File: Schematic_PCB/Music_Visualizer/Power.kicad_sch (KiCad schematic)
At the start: 38 parts, among them J2 Barrel_Jack_PTH, J6 3.5mm, Q1 DMP2123LQ-7, SW2 SW_SPST, U1 LM324, U2 LM324, U3 LM324, U4 LM324, U5 LM324, U6 LM324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

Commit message: Replace elec. cap.
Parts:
- C54: footprint Capacitor_THT:CP_Radial_D5.0mm_P2.00mm -> Capacitor_SMD:CP_Elec_6.3x5.3
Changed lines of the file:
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@@
 			)
 		)
-		(property "Footprint" "Capacitor_THT:CP_Radial_D5.0mm_P2.00mm"
+		(property "Footprint" "Capacitor_SMD:CP_Elec_6.3x5.3"
 			(at 50.4952 54.61 0)
 			(effects

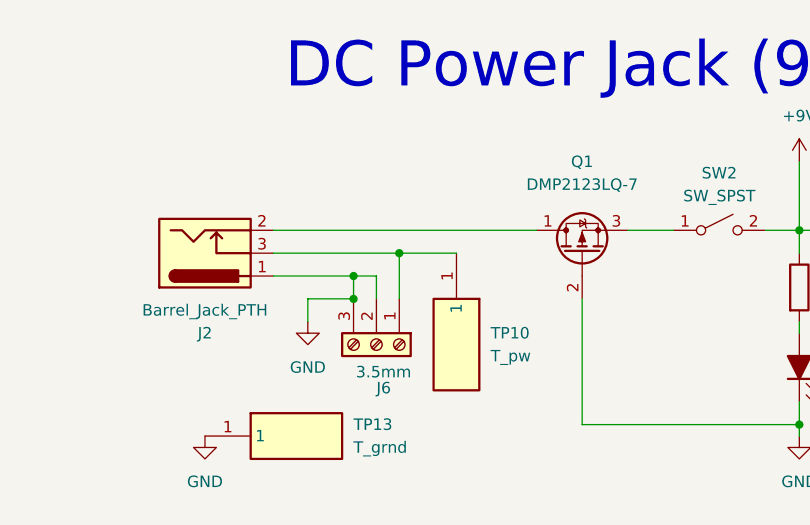
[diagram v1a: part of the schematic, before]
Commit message: Change Barrel jack footprint
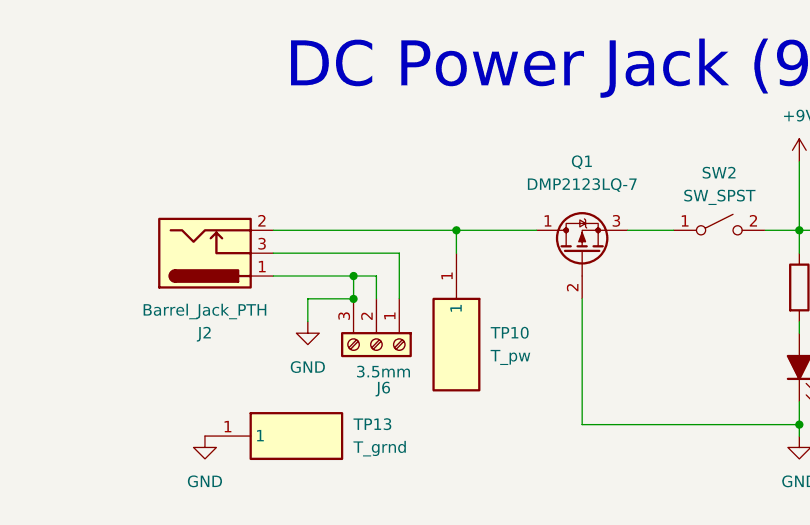
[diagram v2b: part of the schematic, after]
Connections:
- net at J2.2 (GND), Q1.1 (D): now also TP10.1
- net at J2.3 (GNDBREAK), J6.1 (Pin_1): no longer TP10.1
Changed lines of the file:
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@@
+	)
+	(junction
+		(at 172.72 52.07)
+		(diameter 0)
+		(color 0 0 0 0)
 	)
 	(junction
@@
 	)
 	(junction
-		(at 166.37 54.61)
-		(diameter 0)
-		(color 0 0 0 0)
-	)
-	(junction
 		(at 210.82 52.07)
 		(diameter 0)
@@
 	(wire
 		(pts
+			(xy 172.72 52.07) (xy 181.61 52.07)
+		)
+		(stroke
+			(width 0)
+			(type default)
+		)
+	)
+	(wire
+		(pts
 			(xy 191.77 52.07) (xy 196.85 52.07)
 		)
@@
 	(wire
 		(pts
+			(xy 172.72 52.07) (xy 172.72 54.61)
+		)
+		(stroke
+			(width 0)
+			(type default)
+		)
+	)
+	(wire
+		(pts
 			(xy 58.42 99.06) (xy 69.85 99.06)
 		)
@@
 	(wire
 		(pts
-			(xy 152.4 52.07) (xy 181.61 52.07)
+			(xy 152.4 52.07) (xy 172.72 52.07)
 		)
 		(stroke
@@
 		)
 		(stroke
-			(width 0)
-			(type default)
-		)
-	)
-	(wire
-		(pts
-			(xy 166.37 54.61) (xy 172.72 54.61)
-		)
-		(stroke

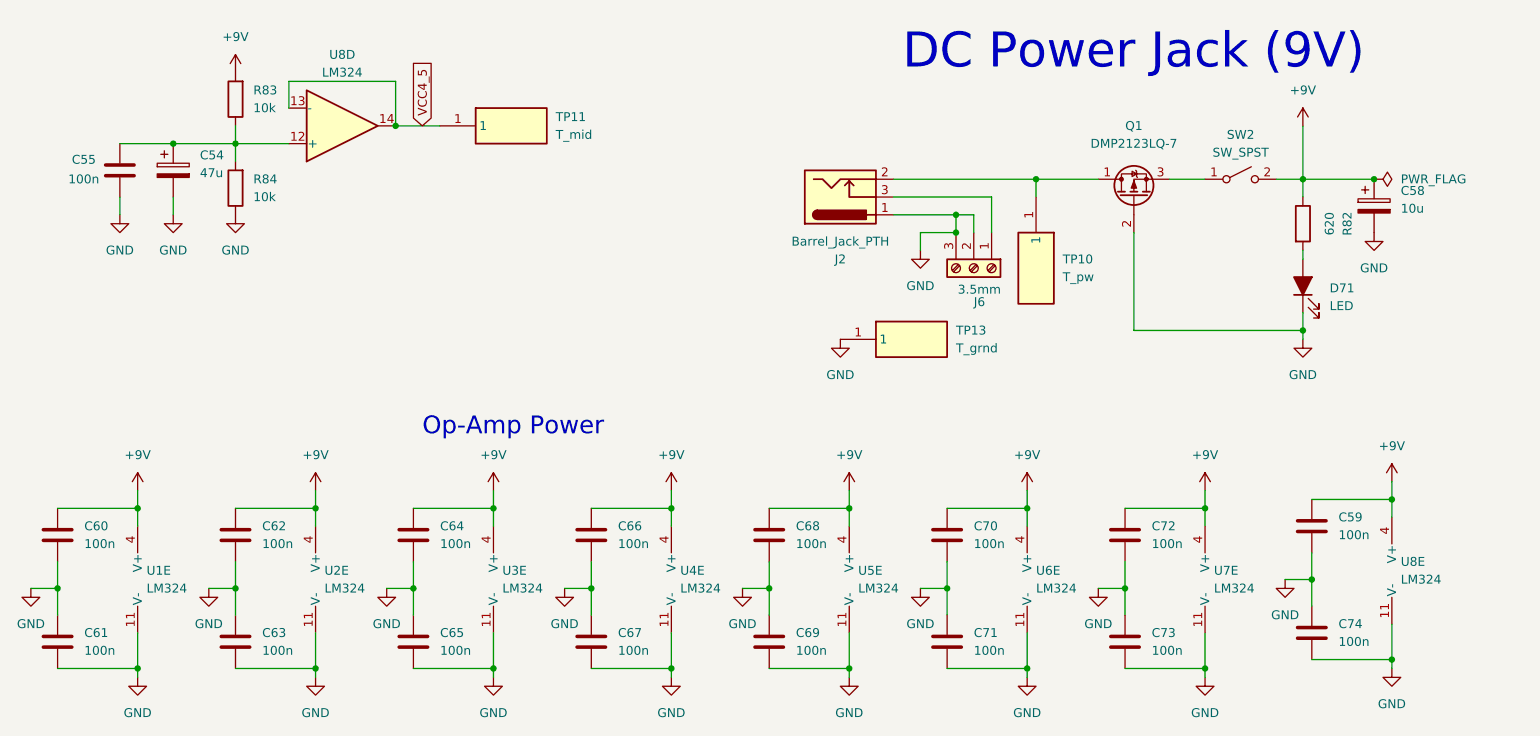
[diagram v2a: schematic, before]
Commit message: Update op amp decoupling
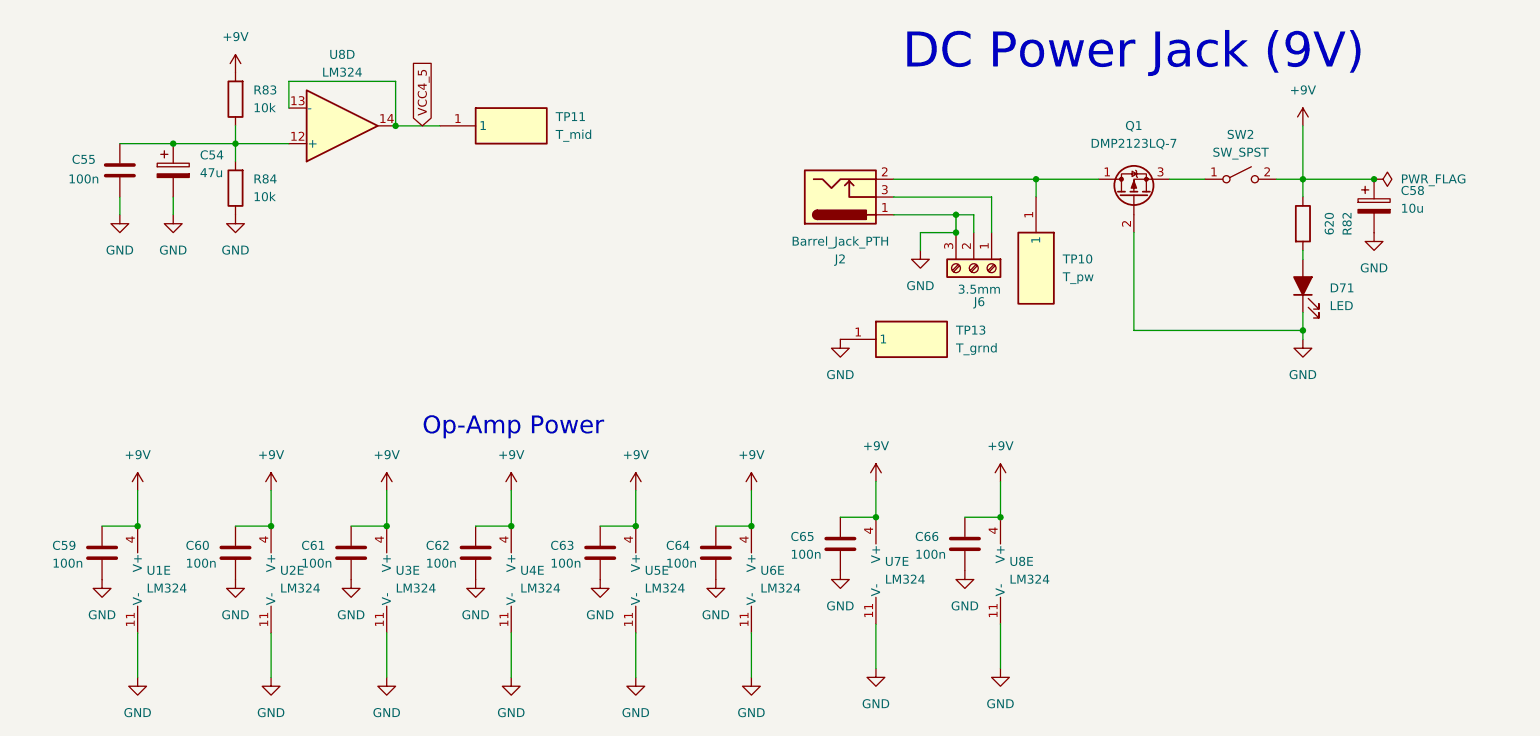
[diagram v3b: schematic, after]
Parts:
- removed C67, C68, C69, C70, C71, C72, C73, C74: 100n, Custom_Footprints:C_0805_2012Metric_Pad1.18x1.45mm_HandSolder, symbol Device:C
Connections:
- net +9V: now also C61.2, C63.2, C65.2
- net GND: no longer C61.2, C63.2, C65.2

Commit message: Remove jacks and compact placement
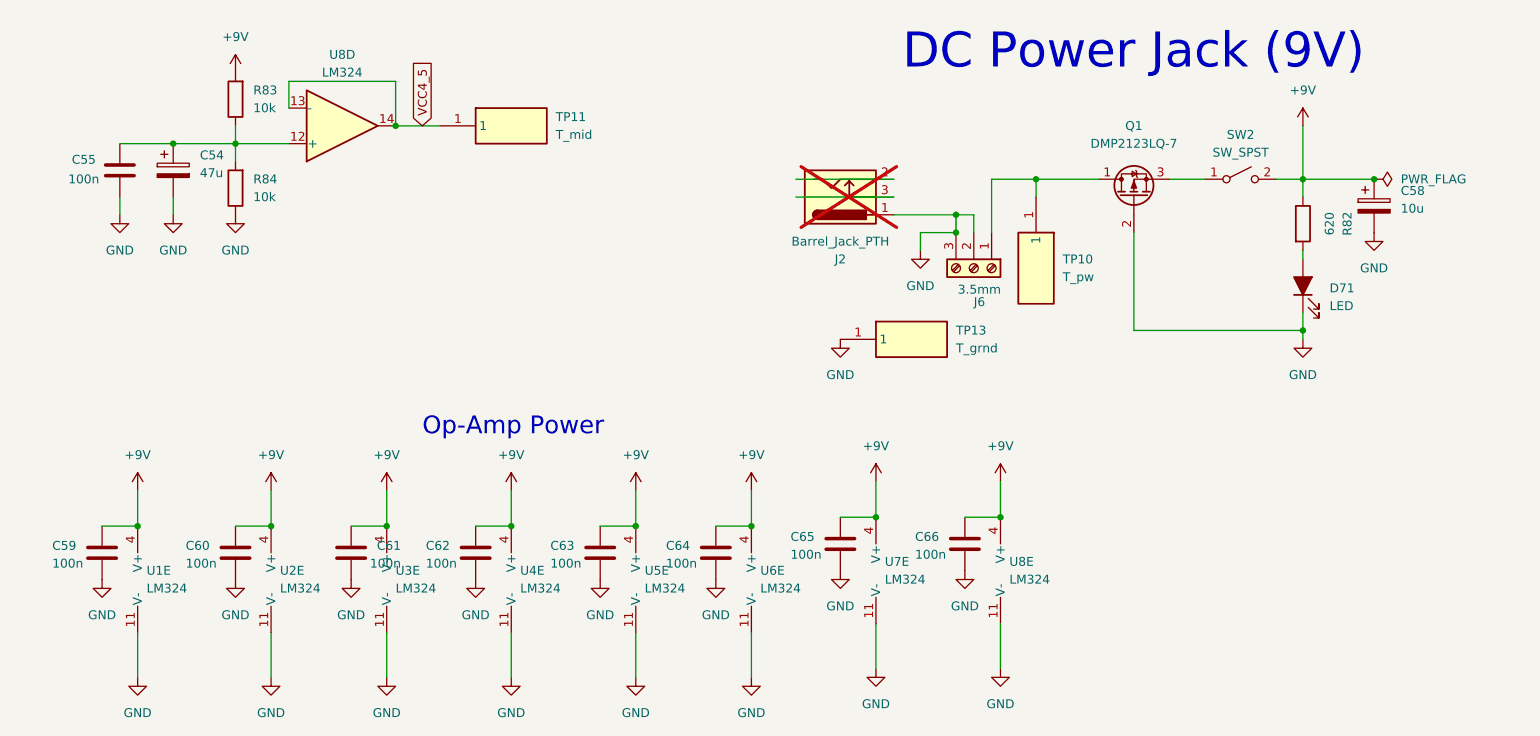
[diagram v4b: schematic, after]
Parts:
- J2: now not fitted; now left out of the parts list
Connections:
- net at Q1.1 (D), TP10.1: now also J6.1 (Pin_1); no longer J2.2 (GND)
- net at J2.3 (GNDBREAK): no longer J6.1 (Pin_1)
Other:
- moved on the sheet: C61
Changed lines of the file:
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@@
 	(wire
 		(pts
-			(xy 166.37 54.61) (xy 166.37 59.69)
-		)
-		(stroke
-			(width 0)
-			(type default)
-		)
-	)
-	(wire
-		(pts
 			(xy 66.04 38.1) (xy 81.28 38.1)
 		)
@@
 	(wire
 		(pts
-			(xy 152.4 54.61) (xy 166.37 54.61)
+			(xy 152.4 54.61) (xy 138.43 54.61)
 		)
 		(stroke
@@
 	(wire
 		(pts
-			(xy 152.4 52.07) (xy 172.72 52.07)
+			(xy 152.4 52.07) (xy 138.43 52.07)
+		)
+		(stroke
+			(width 0)
+			(type default)
+		)
+	)
+	(wire
+		(pts
+			(xy 166.37 52.07) (xy 166.37 59.69)
+		)
+		(stroke
+			(width 0)
+			(type default)
+		)
+	)
+	(wire
+		(pts
+			(xy 166.37 52.07) (xy 172.72 52.07)
 		)
 		(stroke
@@
 	(symbol
 		(lib_id "Device:C")
-		(at 74.93 105.41 180)
+		(at 74.93 105.41 0)
+		(mirror x)
 		(unit 1)
 		(exclude_from_sim no)
@@
 		(dnp no)
 		(property "Reference" "C61"
-			(at 67.818 104.394 0)
+			(at 82.042 104.394 0)
 			(effects
 				(font
@@
 		)
 		(property "Value" "100n"
-			(at 67.818 106.934 0)
+			(at 82.042 106.934 0)
 			(effects
 				(font
@@
 		)
 		(property "Footprint" "Custom_Footprints:C_0805_2012Metric_Pad1.18x1.45mm_HandSolder"
-			(at 73.9648 101.6 0)
+			(at 75.8952 101.6 0)
 			(effects
 				(font
@@
 		(unit 1)
 		(exclude_from_sim no)
-		(in_bom yes)
-		(on_board yes)
-		(dnp no)
+		(in_bom no)
+		(on_board no)
+		(dnp yes)
 		(property "Reference" "J2"
 			(at 144.78 63.5 0)
@@
 		(lib_id "power:+9V")
 		(at 210.82 44.45 0)
+		(mirror y)
 		(unit 1)
 		(exclude_from_sim no)
@@
 		(on_board yes)
 		(dnp no)
-		(fields_autoplaced yes)
 		(property "Reference" "#PWR045"
 			(at 210.82 48.26 0)

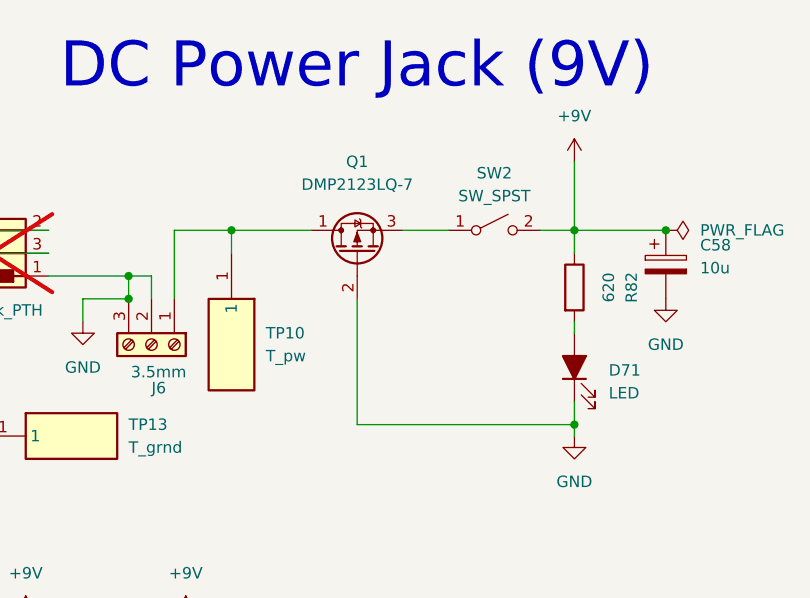
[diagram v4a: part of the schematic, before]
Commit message: Refine traces layout
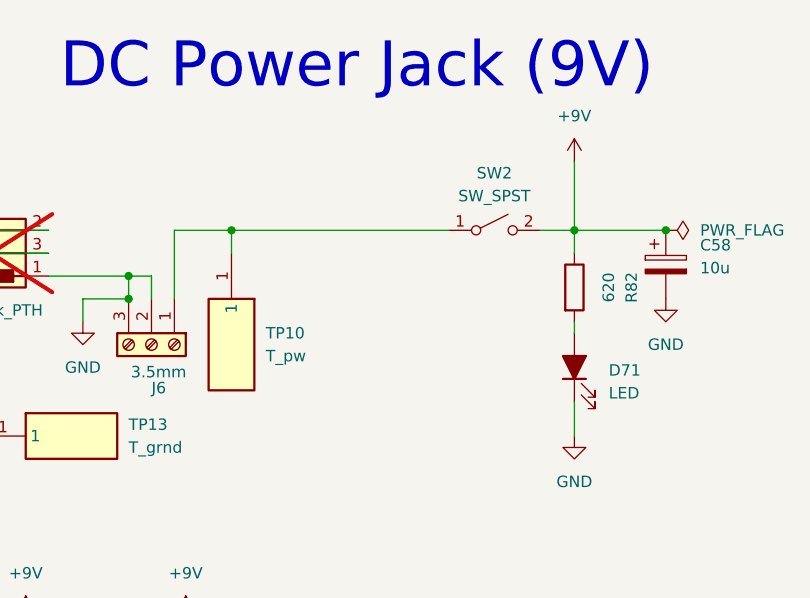
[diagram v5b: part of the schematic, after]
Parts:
- removed Q1: DMP2123LQ-7, Package_TO_SOT_SMD:SOT-23, symbol Device:Q_PMOS_DGS
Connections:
- net at SW2.1 (A): now also J6.1 (Pin_1), TP10.1

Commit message: pre RDC
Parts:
- added Q1: DMP2123LQ-7, Package_TO_SOT_SMD:SOT-23, symbol Device:Q_PMOS_DGS
- C55, C59, C60, C61, C62, C63, C64, C65, C66: footprint Custom_Footprints:C_0805_2012Metric_Pad1.18x1.45mm_HandSolder -> Custom_Footprints:custom_C_0805_2012Metric_Pad1.18x1.45mm_HandSolder
- C58: footprint Capacitor_THT:CP_Radial_D5.0mm_P2.00mm -> Capacitor_SMD:CP_Elec_4x5.4
- D71: footprint LED_SMD:LED_1210_3225Metric_Pad1.42x2.65mm_HandSolder -> PCM_SparkFun-LED:LED_1206_3216Metric_Red
- J6: footprint PCM_SparkFun-Connector:ScrewTerminal_1x03_P3.5mm_Horizontal_Black -> Connector_JST:JST_EH_B2B-EH-A_1x02_P2.50mm_Vertical; symbol PCM_SparkFun-Connector:ScrewTerminal_1x03_P3.5mm_Horizontal_Black -> PCM_SparkFun-Connector:Conn_01x02_JST_P2.0mm_Horizontal_SMD; PROD_ID CONN-08288 -> CONN-11443
- T_gnd1: renamed from TP13; value T_grnd -> T_gnd; footprint Custom_Footprints:TEST1Y -> Custom_Footprints:NEW_2_TestPoint_Loop_D2.60mm_Drill0.9mm_Beaded
- T_mid1: renamed from TP11; footprint Custom_Footprints:TEST1Y -> Custom_Footprints:NEW_2_TestPoint_Loop_D2.60mm_Drill0.9mm_Beaded
- T_pw1: renamed from TP10; footprint Custom_Footprints:TEST1Y -> Custom_Footprints:NEW_2_TestPoint_Loop_D2.60mm_Drill0.9mm_Beaded
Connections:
- net GND: now also J6.1 (-), Q1.2 (G); no longer J6.2 (Pin_2), J6.3 (Pin_3)
- new net: Q1.3 (S), SW2.1 (A)
- new net: J6.2 (+), Q1.1 (D), T_pw1.1
